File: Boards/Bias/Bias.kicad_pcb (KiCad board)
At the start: 2 copper layers, 80 x 50 mm, 39 parts, among them P1 CONN_12V, P2 CONN_R, U1 LM339

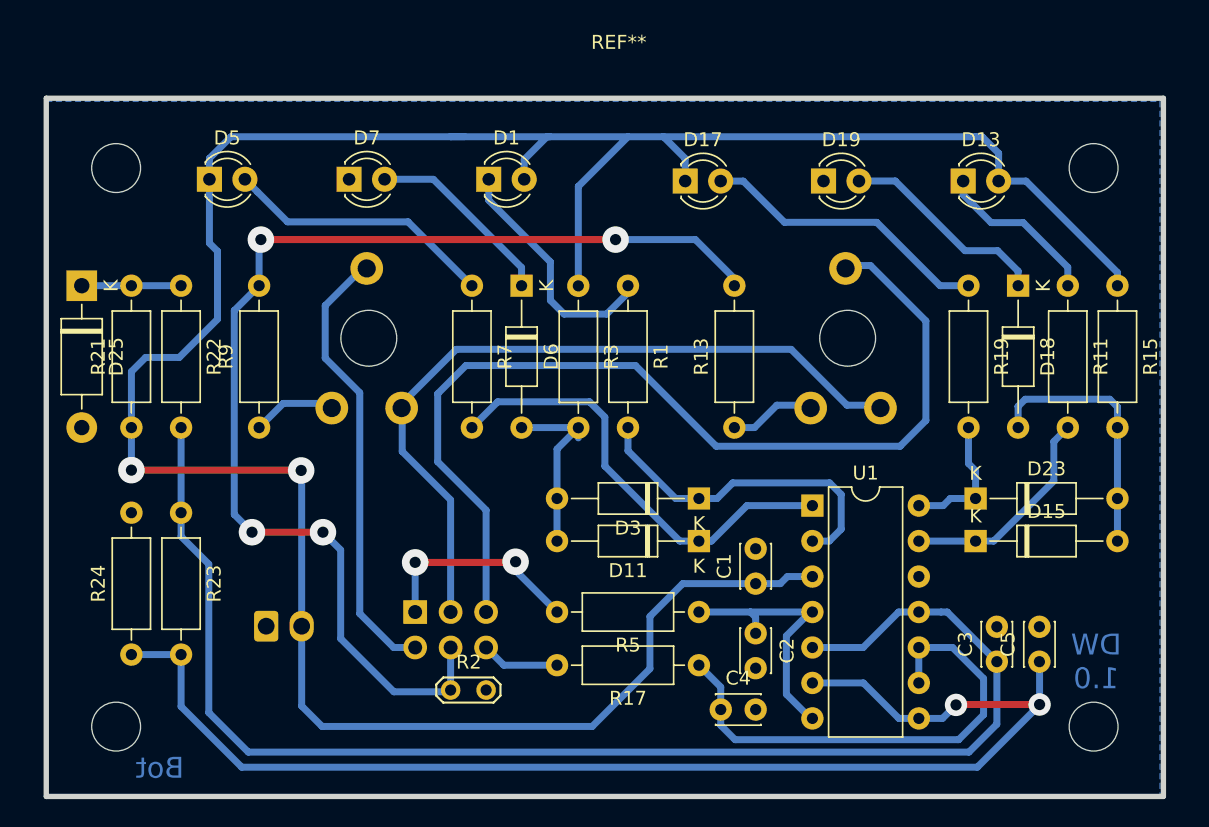
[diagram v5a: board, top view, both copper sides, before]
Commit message: HV Switch on delay added
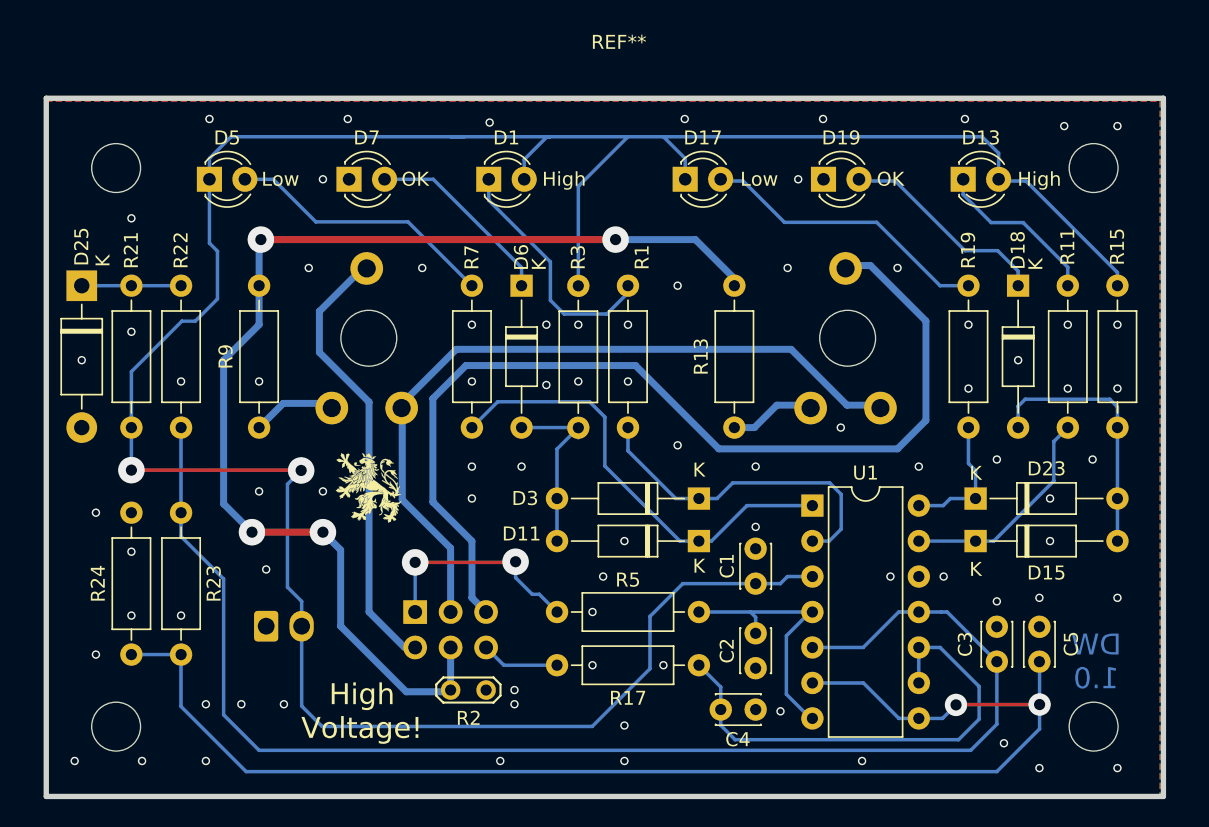
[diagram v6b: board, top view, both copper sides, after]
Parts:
- added G***: LOGO, Loewe:Loewe_Klein, F.Cu at (163.3, 90.2)
- moved D13 0.13 mm to (205.9, 68.1)
- moved D17 0.13 mm to (186.0, 68.1)
- moved D19 0.13 mm to (195.9, 68.1)
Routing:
- net REF_L: track 93.2 -> 94.5 mm
- net Net-(C4-Pad1): track 35.6 -> 34.8 mm
- net REF_H: track 99.9 -> 99.2 mm
- net GND: vias 0 -> 80
- net (no net): vias 0 -> 1
- added copper zone on F.Cu, net GND
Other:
- board text added: "Do not disconnect while powered!"
- board text added: "High"
- board text added: "High Voltage!"
- board text added: "Low"
- board text added: "OK"
- board text removed: "Bot"

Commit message: Added Vias & Mounting Holes
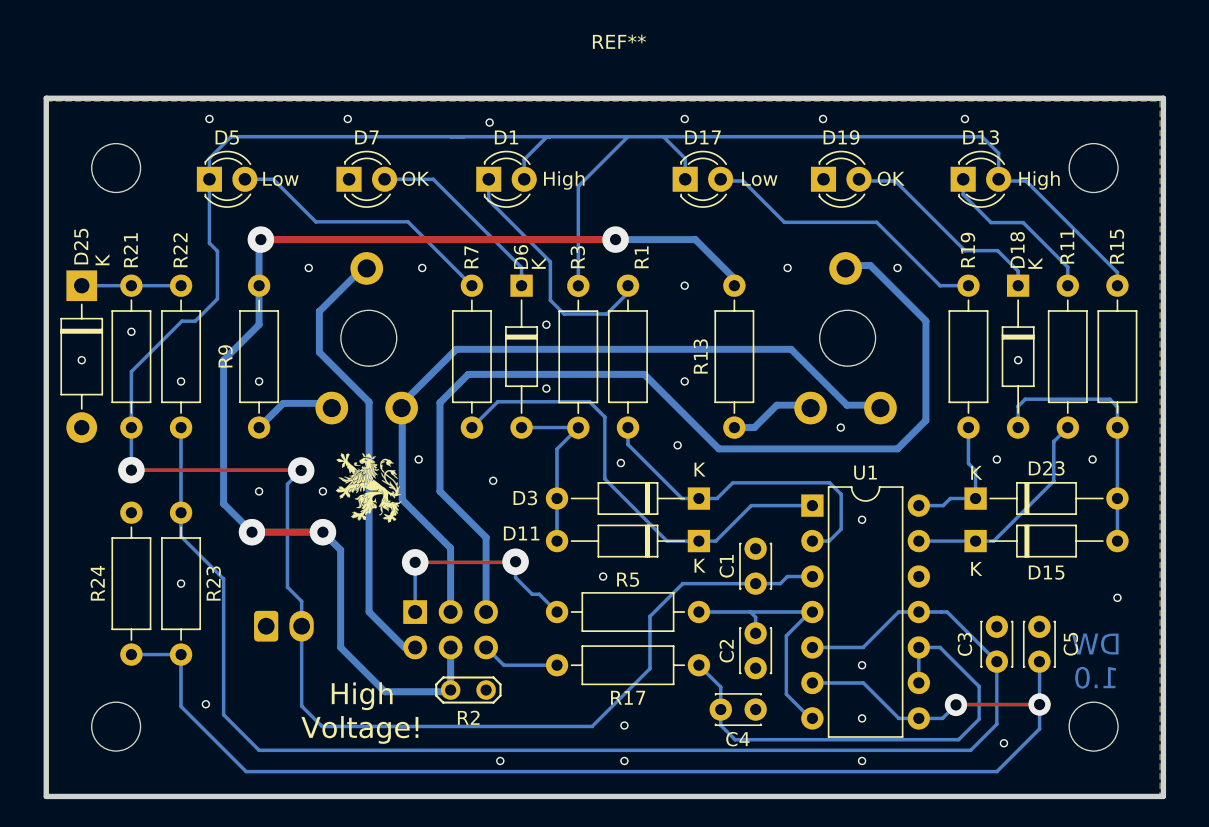
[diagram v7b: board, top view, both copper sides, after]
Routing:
- net /UG_R2: track 71.2 -> 69.8 mm
- net GNDS: track 83.7 -> 84.6 mm
- net Net-(D11-Pad1): track 33.1 -> 33.6 mm
- net GND: vias 80 -> 40
- net (no net): vias 1 -> 0

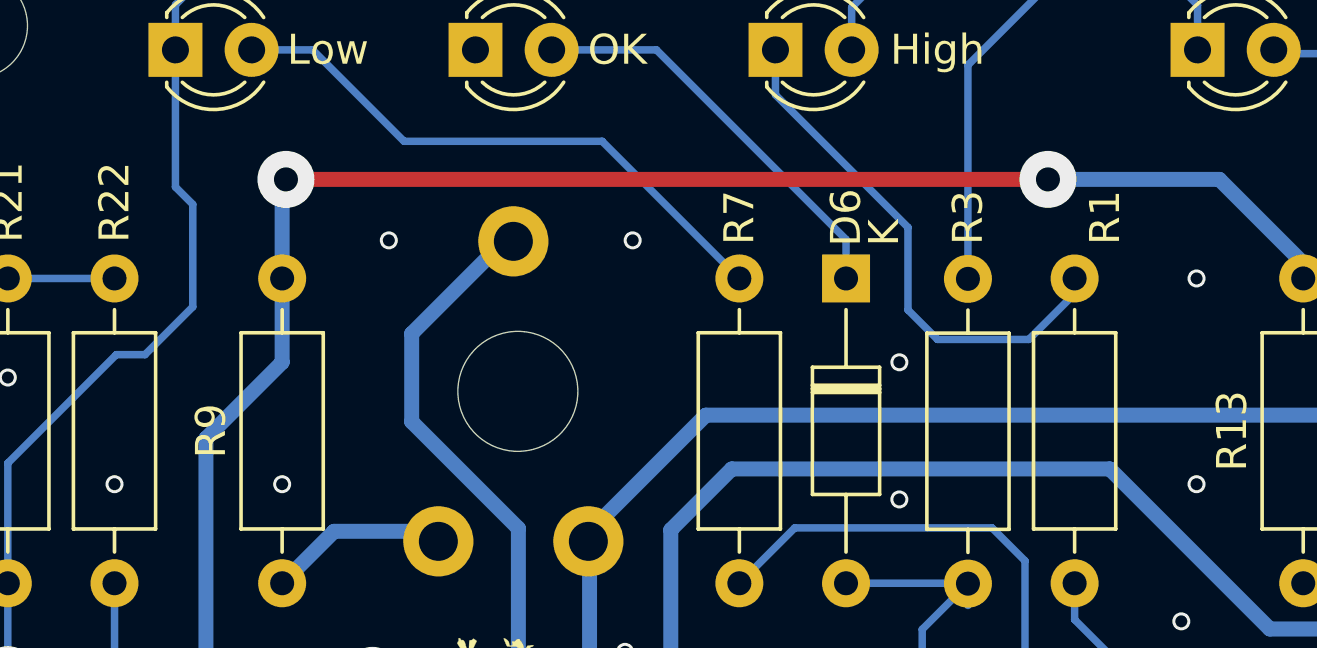
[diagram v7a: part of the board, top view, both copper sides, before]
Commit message: Adjusted Silkscreen
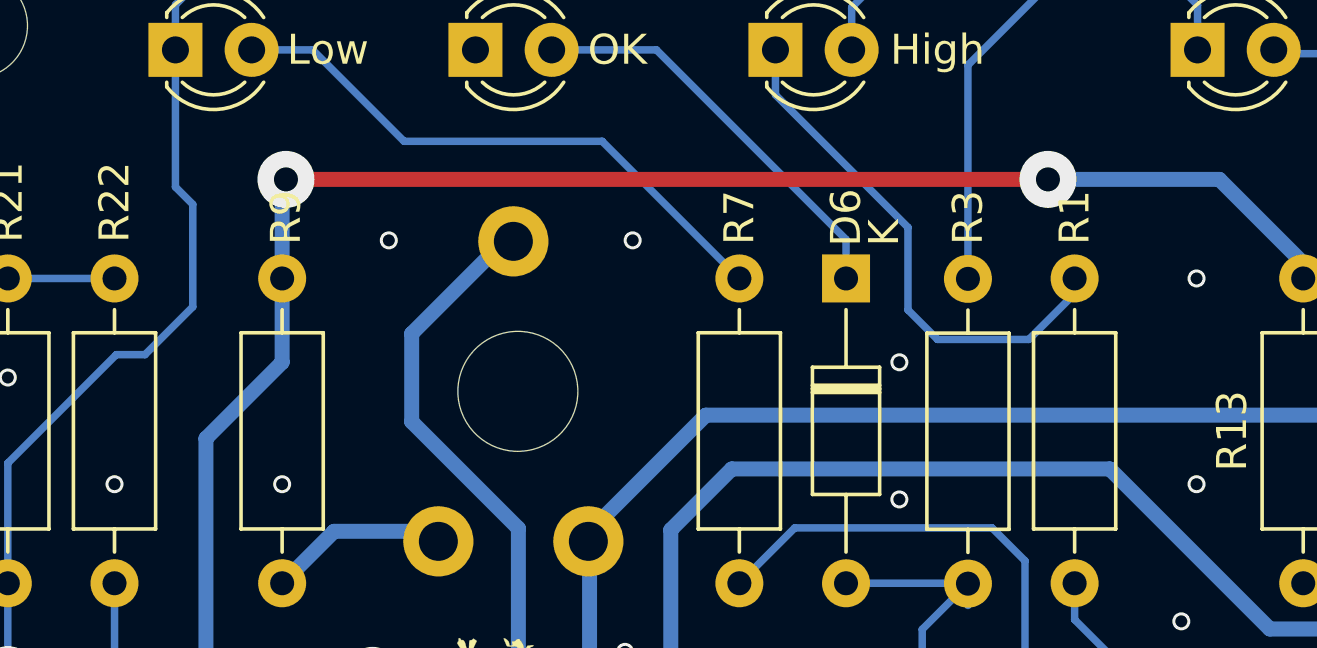
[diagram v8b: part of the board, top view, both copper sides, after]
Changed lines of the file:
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@@
   (page A4)
   (layers
-    (0 F.Cu signal)
-    (31 B.Cu signal)
+    (0 F.Cu signal hide)
+    (31 B.Cu signal hide)
     (32 B.Adhes user)
     (33 F.Adhes user)
@@
     (47 F.CrtYd user)
     (48 B.Fab user)
-    (49 F.Fab user)
+    (49 F.Fab user hide)
   )
   (setup
@@
     (descr "Resistor, Axial_DIN0207 series, Axial, Horizontal, pin pitch=10.16mm, 0.25W = 1/4W, length*diameter=6.3*2.5mm^2, http://cdn-reichelt.de/documents/datenblatt/B400/1_4W%23YAG.pdf")
     (tags "Resistor Axial_DIN0207 series Axial Horizontal pin pitch 10.16mm 0.25W = 1/4W length 6.3mm diameter 2.5mm")
-    (fp_text reference R9 (at 5.08 -2.37 90) (layer F.SilkS)
+    (fp_text reference R9 (at 12.192 0.127 90) (layer F.SilkS)
       (effects (font (size 1 1) (thickness 0.15)))
     )
@@
     (descr "Resistor, Axial_DIN0207 series, Axial, Horizontal, pin pitch=10.16mm, 0.25W = 1/4W, length*diameter=6.3*2.5mm^2, http://cdn-reichelt.de/documents/datenblatt/B400/1_4W%23YAG.pdf")
     (tags "Resistor Axial_DIN0207 series Axial Horizontal pin pitch 10.16mm 0.25W = 1/4W length 6.3mm diameter 2.5mm")
-    (fp_text reference R1 (at -2.032 -1.016 270) (layer F.SilkS)
-      (effects (font (size 1 1) (thickness 0.15)))
-    )
+    (fp_text reference R1 (at -2.032 0 270) (layer F.SilkS)
+      (effects (font (size 1 1) (thickness 0.15)))
+    )
